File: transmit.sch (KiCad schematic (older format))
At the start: 26 parts, among them U13 74HC86, U14 74HC164, U15 27C128, U17 74HC74, U18 74HC164, U19 ZN429E-8

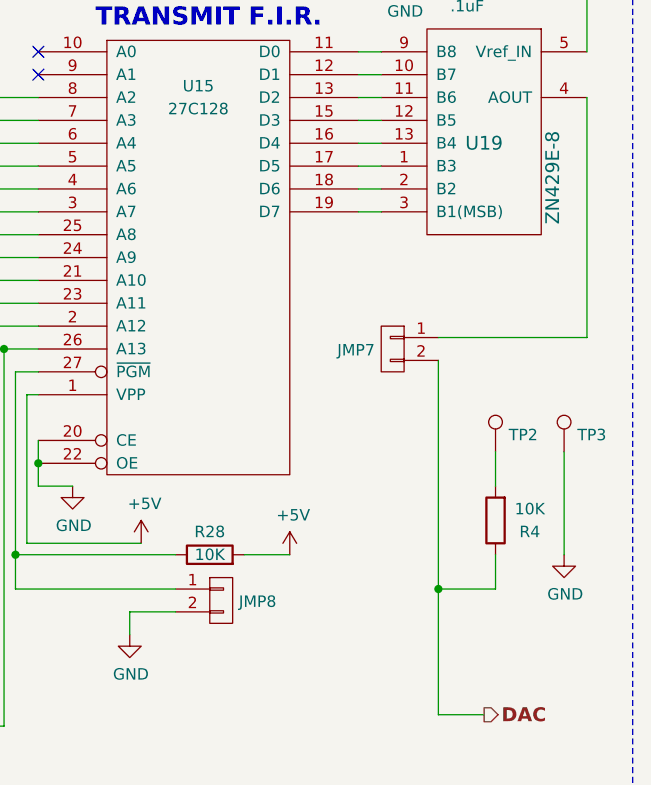
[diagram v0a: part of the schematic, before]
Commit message: Final parts placement and verified net against an actual Issue 3 board.
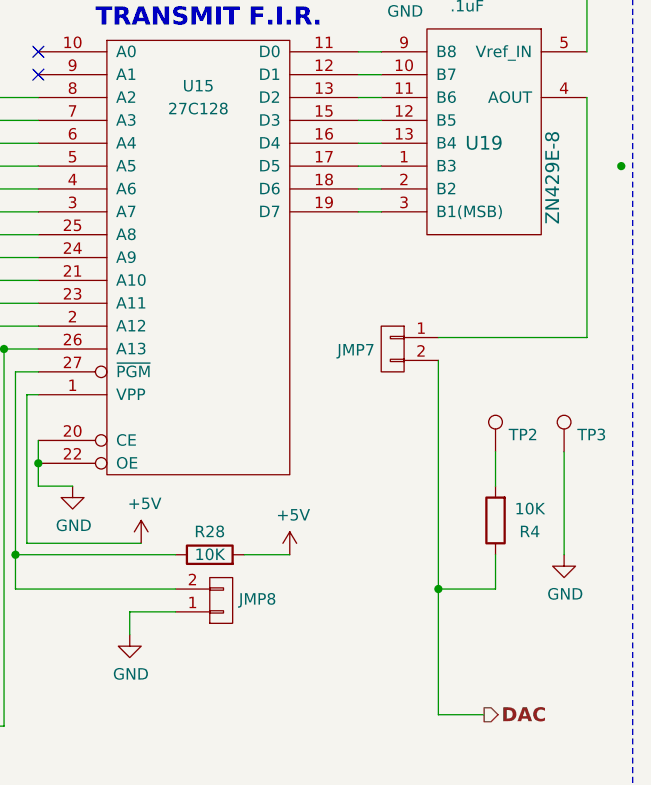
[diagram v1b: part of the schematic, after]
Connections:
- net GND: now also JMP8.1 (P1); no longer JMP8.2 (P2)
- net at R28.1, U15.27 (~PGM): now also JMP8.2 (P2); no longer JMP8.1 (P1)
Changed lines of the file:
@@
 $EndComp
 $Comp
-L +5V #PWR059
+L +5V #PWR058
 U 1 1 59860A94
 P 2300 3500
-F 0 "#PWR059" H 2300 3350 50  0001 C CNN
+F 0 "#PWR058" H 2300 3350 50  0001 C CNN
 F 1 "+5V" H 2315 3673 50  0000 C CNN
 F 2 "" H 2300 3500 50  0001 C CNN
@@
 $EndComp
 $Comp
-L +5V #PWR060
+L +5V #PWR059
 U 1 1 59860A9A
 P 2100 2350
-F 0 "#PWR060" H 2100 2200 50  0001 C CNN
+F 0 "#PWR059" H 2100 2200 50  0001 C CNN
 F 1 "+5V" H 2115 2523 50  0000 C CNN
 F 2 "" H 2100 2350 50  0001 C CNN
@@
 $EndComp
 $Comp
-L +5V #PWR061
+L +5V #PWR060
 U 1 1 59860AAE
 P 3850 2500
-F 0 "#PWR061" H 3850 2350 50  0001 C CNN
+F 0 "#PWR060" H 3850 2350 50  0001 C CNN
 F 1 "+5V" H 3865 2673 50  0000 C CNN
 F 2 "" H 3850 2500 50  0001 C CNN
@@
 $EndComp
 $Comp
-L GND #PWR062
+L GND #PWR061
 U 1 1 59860AB4
 P 3300 3100
-F 0 "#PWR062" H 3300 2850 50  0001 C CNN
+F 0 "#PWR061" H 3300 2850 50  0001 C CNN
 F 1 "GND" H 3305 2927 50  0000 C CNN
 F 2 "" H 3300 3100 50  0001 C CNN
@@
 $EndComp
 $Comp
-L +5V #PWR063
+L +5V #PWR062
 U 1 1 59860AD7
 P 5550 2900
-F 0 "#PWR063" H 5550 2750 50  0001 C CNN
+F 0 "#PWR062" H 5550 2750 50  0001 C CNN
 F 1 "+5V" H 5565 3073 50  0000 C CNN
 F 2 "" H 5550 2900 50  0001 C CNN
@@
 $EndComp
 $Comp
-L +5V #PWR064
+L +5V #PWR063
 U 1 1 59860ADD
 P 3750 3150
-F 0 "#PWR064" H 3750 3000 50  0001 C CNN
+F 0 "#PWR063" H 3750 3000 50  0001 C CNN
 F 1 "+5V" H 3765 3323 50  0000 C CNN
 F 2 "" H 3750 3150 50  0001 C CNN
@@
 $EndComp
 $Comp
-L +5V #PWR065
+L +5V #PWR064
 U 1 1 59860AEB
 P 5300 4100
-F 0 "#PWR065" H 5300 3950 50  0001 C CNN
+F 0 "#PWR064" H 5300 3950 50  0001 C CNN
 F 1 "+5V" H 5315 4273 50  0000 C CNN
 F 2 "" H 5300 4100 50  0001 C CNN
@@
 $EndComp
 $Comp
-L GND #PWR066
+L GND #PWR065
 U 1 1 59860B0D
 P 7950 4150
-F 0 "#PWR066" H 7950 3900 50  0001 C CNN
+F 0 "#PWR065" H 7950 3900 50  0001 C CNN
 F 1 "GND" H 7955 3977 50  0000 C CNN
 F 2 "" H 7950 4150 50  0001 C CNN
@@
 $EndComp
 $Comp
-L +5V #PWR067
+L +5V #PWR066
 U 1 1 59860B1A
 P 9550 4500
-F 0 "#PWR067" H 9550 4350 50  0001 C CNN
+F 0 "#PWR066" H 9550 4350 50  0001 C CNN
 F 1 "+5V" H 9565 4673 50  0000 C CNN
 F 2 "" H 9550 4500 50  0001 C CNN
@@
 $EndComp
 $Comp
-L GND #PWR068
+L GND #PWR067
 U 1 1 59860B20
 P 7950 4550
-F 0 "#PWR068" H 7950 4300 50  0001 C CNN
+F 0 "#PWR067" H 7950 4300 50  0001 C CNN
 F 1 "GND" H 7955 4377 50  0000 C CNN
 F 2 "" H 7950 4550 50  0001 C CNN
@@
 $EndComp
 $Comp
-L GND #PWR069
+L GND #PWR068
 U 1 1 59860B34
 P 7950 4950
-F 0 "#PWR069" H 7950 4700 50  0001 C CNN
+F 0 "#PWR068" H 7950 4700 50  0001 C CNN
 F 1 "GND" H 7955 4777 50  0000 C CNN
 F 2 "" H 7950 4950 50  0001 C CNN
@@
 $EndComp
 $Comp
-L GND #PWR070
+L GND #PWR069
 U 1 1 59860B41
 P 7950 5350
-F 0 "#PWR070" H 7950 5100 50  0001 C CNN
+F 0 "#PWR069" H 7950 5100 50  0001 C CNN
 F 1 "GND" H 7955 5177 50  0000 C CNN
 F 2 "" H 7950 5350 50  0001 C CNN
@@
 $EndComp
 $Comp
-L +5V #PWR071
+L +5V #PWR070
 U 1 1 59860B4E
 P 10850 2050
-F 0 "#PWR071" H 10850 1900 50  0001 C CNN
+F 0 "#PWR070" H 10850 1900 50  0001 C CNN
 F 1 "+5V" H 10865 2223 50  0000 C CNN
 F 2 "" H 10850 2050 50  0001 C CNN
@@
 $EndComp
 $Comp
-L GND #PWR072
+L GND #PWR071
 U 1 1 59860B54
 P 8850 4850
-F 0 "#PWR072" H 8850 4600 50  0001 C CNN
+F 0 "#PWR071" H 8850 4600 50  0001 C CNN
 F 1 "GND" H 8855 4677 50  0000 C CNN
 F 2 "" H 8850 4850 50  0001 C CNN
@@
 F 3 "" H 9250 4700 50  0001 C CNN
 	1    9250 4700
-	1    0    0    -1
+	1    0    0    1
 $EndComp
 $Comp
@@
 $EndComp
 $Comp
-L +5V #PWR073
+L +5V #PWR072
 U 1 1 59860B68
 P 8900 4450
-F 0 "#PWR073" H 8900 4300 50  0001 C CNN
+F 0 "#PWR072" H 8900 4300 50  0001 C CNN
 F 1 "+5V" H 8915 4623 50  0000 C CNN
 F 2 "" H 8900 4450 50  0001 C CNN
@@
 $EndComp
 $Comp
-L GND #PWR074
+L GND #PWR073
 U 1 1 59860B6E
 P 8600 4200
-F 0 "#PWR074" H 8600 3950 50  0001 C CNN
+F 0 "#PWR073" H 8600 3950 50  0001 C CNN
 F 1 "GND" H 8605 4027 50  0000 C CNN
 F 2 "" H 8600 4200 50  0001 C CNN
@@
 $EndComp
 $Comp
-L +5V #PWR075
+L +5V #PWR074
 U 1 1 59860B74
 P 3850 4650
-F 0 "#PWR075" H 3850 4500 50  0001 C CNN
+F 0 "#PWR074" H 3850 4500 50  0001 C CNN
 F 1 "+5V" H 3865 4823 50  0000 C CNN
 F 2 "" H 3850 4650 50  0001 C CNN
@@
 $EndComp
 $Comp
-L +5V #PWR076
+L +5V #PWR075
 U 1 1 59860B7A
 P 3700 3700
-F 0 "#PWR076" H 3700 3550 50  0001 C CNN
+F 0 "#PWR075" H 3700 3550 50  0001 C CNN
 F 1 "+5V" H 3715 3873 50  0000 C CNN
 F 2 "" H 3700 3700 50  0001 C CNN
@@
 TRANSMIT F.I.R.
 $Comp
-L +5V #PWR077
+L +5V #PWR076
 U 1 1 59860B81
 P 7450 3600
-F 0 "#PWR077" H 7450 3450 50  0001 C CNN
+F 0 "#PWR076" H 7450 3450 50  0001 C CNN
 F 1 "+5V" H 7465 3773 50  0000 C CNN
 F 2 "" H 7450 3600 50  0001 C CNN
@@
 $EndComp
 $Comp
-L GND #PWR078
+L GND #PWR077
 U 1 1 59860C2C
 P 10750 4500
-F 0 "#PWR078" H 10750 4250 50  0001 C CNN
+F 0 "#PWR077" H 10750 4250 50  0001 C CNN
 F 1 "GND" H 10755 4327 50  0000 C CNN
 F 2 "" H 10750 4500 50  0001 C CNN
@@
 $EndComp
 $Comp
-L +5V #PWR079
+L +5V #PWR078
 U 1 1 598A2AE8
 P 10650 1950
-F 0 "#PWR079" H 10650 1800 50  0001 C CNN
+F 0 "#PWR078" H 10650 1800 50  0001 C CNN
 F 1 "+5V" H 10665 2123 50  0000 C CNN
 F 2 "" H 10650 1950 50  0001 C CNN
@@
 $EndComp
 $Comp
-L GND #PWR080
+L GND #PWR079
 U 1 1 598A2D96
 P 10050 1950
-F 0 "#PWR080" H 10050 1700 50  0001 C CNN
+F 0 "#PWR079" H 10050 1700 50  0001 C CNN
 F 1 "GND" H 10055 1777 50  0000 C CNN
 F 2 "" H 10050 1950 50  0001 C CNN
@@
 $EndComp
 $Comp
-L +5V #PWR081
+L +5V #PWR080
 U 1 1 598A3E23
 P 5600 3600
-F 0 "#PWR081" H 5600 3450 50  0001 C CNN
+F 0 "#PWR080" H 5600 3450 50  0001 C CNN
 F 1 "+5V" H 5615 3773 50  0000 C CNN
 F 2 "" H 5600 3600 50  0001 C CNN
@@
 $EndComp
 $Comp
-L GND #PWR082
+L GND #PWR081
 U 1 1 598A3FA6
 P 5600 4000
-F 0 "#PWR082" H 5600 3750 50  0001 C CNN
+F 0 "#PWR081" H 5600 3750 50  0001 C CNN
 F 1 "GND" H 5605 3827 50  0000 C CNN
 F 2 "" H 5600 4000 50  0001 C CNN
@@
 $EndComp
 $Comp
-L +5V #PWR083
+L +5V #PWR082
 U 1 1 598A48CD
 P 8250 2200
-F 0 "#PWR083" H 8250 2050 50  0001 C CNN
+F 0 "#PWR082" H 8250 2050 50  0001 C CNN
 F 1 "+5V" H 8265 2373 50  0000 C CNN
 F 2 "" H 8250 2200 50  0001 C CNN
@@
 $EndComp
 $Comp
-L GND #PWR084
+L GND #PWR083
 U 1 1 598A492F
 P 7650 2200
-F 0 "#PWR084" H 7650 1950 50  0001 C CNN
+F 0 "#PWR083" H 7650 1950 50  0001 C CNN
 F 1 "GND" H 7655 2027 50  0000 C CNN
 F 2 "" H 7650 2200 50  0001 C CNN
@@
 Wire Wire Line
 	7800 2200 7650 2200
+Connection ~ 11000 2800
 $EndSCHEMATC
